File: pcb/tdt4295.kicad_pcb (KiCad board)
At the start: 6 copper layers, 94.8 x 111 mm, 158 parts, among them J1 DE15_Socket_HighDensity, J2 Conn_02x04_Odd_Even, J3 Conn_ST_STDC14, J4 Micro_SD_Card, J5 USB4110-GF-A, J6 USB4110-GF-A, SW1 SW_BLUE, SW2 SW_BLACK, U1 XC7A50T-FTG256, U2 410-251-B, U3 S70KL1283DPBHV020, U4 W25Q128JVS, U5 TPS54325PWP.d, U6 TPS54294PWP, U7 STM32U595ZJTx, U8 TPS2051CDBV, U9 USBLC6-2SC6, Y1 ASE-20MHz, Y2 16MHz

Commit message: pcb/layout: usbs and pds
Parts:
- removed C62, C71, C72, C74: 100nF, Capacitor_SMD:C_0805_2012Metric_Pad1.18x1.45mm_HandSolder
- removed C73: 1uF, Capacitor_SMD:C_0805_2012Metric_Pad1.18x1.45mm_HandSolder
- removed C75: 0.1uF, Capacitor_SMD:C_0805_2012Metric_Pad1.18x1.45mm_HandSolder
- removed C76: 150uF, Capacitor_SMD:C_0805_2012Metric_Pad1.18x1.45mm_HandSolder
- removed FB1: FerriteBead, Inductor_SMD:L_0805_2012Metric_Pad1.05x1.20mm_HandSolder
- removed J6: USB4110-GF-A, USB4110_GF_A:USB4110-GF-A_GCT
- removed R42, R43: 47, Resistor_SMD:R_0805_2012Metric_Pad1.20x1.40mm_HandSolder
- removed U9: USBLC6-2SC6, Package_TO_SOT_SMD:SOT-23-6
- added D5: green?, LED_SMD:LED_0805_2012Metric_Pad1.15x1.40mm_HandSolder, F.Cu at (55.5, 133.0)
- added D6: red?, LED_SMD:LED_0805_2012Metric_Pad1.15x1.40mm_HandSolder, F.Cu at (55.5, 130.0)
- added D7: LED_ARGB, LED_ARGB:SON4_APTF1616LSEEZGKQBKC_KNB, F.Cu at (263.4, 42.5)
- added D8: red, LED_SMD:LED_0805_2012Metric_Pad1.15x1.40mm_HandSolder, F.Cu at (55.4, 127.0)
- added J7: USB_C_Receptacle_USB2.0_14P, Connector_USB:USB_C_Receptacle_GCT_USB4105-xx-A_16P_TopMnt_Horizontal, F.Cu at (56.0, 116.0)
- added J8: USB_C_Receptacle_USB2.0_14P, Connector_USB:USB_C_Receptacle_GCT_USB4105-xx-A_16P_TopMnt_Horizontal, F.Cu at (56.0, 100.5)
- added R56: 22, Resistor_SMD:R_0805_2012Metric_Pad1.20x1.40mm_HandSolder, F.Cu at (253.8, 63.8)
- added R57: 1k, Resistor_SMD:R_0805_2012Metric_Pad1.20x1.40mm_HandSolder, F.Cu at (60.5, 127.0)
- added R58: 5.1k, Resistor_SMD:R_0805_2012Metric_Pad1.20x1.40mm_HandSolder, F.Cu at (65.0, 117.0)
- added R59: 5.1k, Resistor_SMD:R_0805_2012Metric_Pad1.20x1.40mm_HandSolder, F.Cu at (65.0, 114.0)
- added R60: 10k, Resistor_SMD:R_0805_2012Metric_Pad1.20x1.40mm_HandSolder, F.Cu at (76.0, 94.5)
- C10, C14, C16, C17, C20, C23, C26, C27, C28, C29, C30, C7, C8, C9: footprint Capacitor_SMD:C_0603_1608Metric_Pad1.08x0.95mm_HandSolder -> Capacitor_SMD:C_0805_2012Metric_Pad1.18x1.45mm_HandSolder; moved to F.Cu
- C11, C12, C13, C15, C18, C19, C21, C22, C24, C25, C3, C4, C5, C50, C51, C52, C53, C54, C55, C56, C57, C58, C59, C6, C60, C61, C66, C67, R51: moved to F.Cu
- C36, C37, C46, C47: moved to B.Cu
- C65: value 100nF -> 4.7uF; moved to F.Cu
- C68: value 1uF -> 100nF; moved to F.Cu
- C69: value 4.7uF -> 0.1uF; moved to F.Cu
- C70: value 1uF -> 150uF; moved to F.Cu
- D2: value green? -> blue?
- D4: value red -> blue?
- J1: value DE15_Socket_HighDensity -> FPGA_DEBUG; footprint Connector_Dsub:DSUB-15_Socket_EdgeMount_P2.77mm -> Connector_PinHeader_2.54mm:PinHeader_2x07_P2.54mm_Vertical
- J2: value Conn_02x04_Odd_Even -> DE15_Socket_HighDensity; footprint Connector_JST:JST_PUD_B08B-PUDSS_2x04_P2.00mm_Vertical -> Connector_Dsub:DSUB-15_Socket_EdgeMount_P2.77mm
- J3: value Conn_ST_STDC14 -> Conn_02x04_Odd_Even; footprint Connector_PinHeader_1.27mm:PinHeader_2x07_P1.27mm_Vertical_SMD -> Connector_JST:JST_PUD_B08B-PUDSS_2x04_P2.00mm_Vertical
- J4: value Micro_SD_Card -> Conn_ST_STDC14; footprint Connector_Card:microSD_HC_Molex_47219-2001 -> Connector_PinHeader_1.27mm:PinHeader_2x07_P1.27mm_Vertical_SMD
- J5: value USB4110-GF-A -> Micro_SD_Card; footprint USB4110_GF_A:USB4110-GF-A_GCT -> Connector_Card:microSD_HC_Molex_47219-2001
- R1: value 4.7k -> 10k
- R10: value 1.0k -> 1.1k
- R12: value 3.9k -> 18k
- R13: value 2.0k -> 9.1k
- R14: value 1.0k -> 4.3k
- R15: value 510 -> 2.2k
- R16: value 3.9k -> 1.1k
- R17: value 2.0k -> 560
- R18: value 1.0k -> 8.2k
- R19: value 510 -> 4.3k
- R2: value 330 -> 10k
- R20: value 100 -> 2.2k
- R21: value 100 -> 1.1k
- R22: value 4.7k -> 510
- R23: value 4.7k -> 1k
- R24: value 2.4k -> 1k
- R25: value 30.1k -> 4.7k
- R26: value 22.1k -> 4.7k
- R27: value 1k -> 2.4k
- R28: value 1k -> 51
- R29: value 6.81k -> 22
- R30: value 22.1k -> 22
- R31: value 100k -> 30.1k
- R32: value 100k -> 22.1k
- R33: value 73.2k -> 1k
- R34: value 22.1k -> 1k
- R35: value 1 -> 1k
- R36: value 330 -> 6.81k
- R37: value 100K -> 22.1k
- R38: value 1OK -> 100k; moved to F.Cu
- R39: value 22 -> 100k
- R4: value 4.7k -> 330
- R40: value 22 -> 73.2k
- R41: value 51 -> 22.1k
- R44: value 47 -> 1OK
- R45: value 47 -> 22
- R47: value 22 -> 51
- R48, R49: value 22 -> 47; moved to F.Cu
- R5, R6: value 10k -> 4.7k
- R50: value 22 -> 47
- R52: value 1k -> 22
- R53, R54: value 5.1k -> 22
- R55: value 10k -> 22
- R7: value 4.7k -> 8.2k
- R8: value 3.9k -> 4.3k
- R9: value 2.0k -> 2.2k
- U2: value 410-251-B -> S70KL1283DPBHV020; footprint 410_251_B:IC11_410-251-B_DGT -> S70KL1283DPBHV020:BGA24C100P5X5_600X800X100
- U3: value S70KL1283DPBHV020 -> W25Q128JVS; footprint S70KL1283DPBHV020:BGA24C100P5X5_600X800X100 -> Package_SO:SOIC-8_5.3x5.3mm_P1.27mm
- U4: value W25Q128JVS -> TPS54325PWP.d; footprint Package_SO:SOIC-8_5.3x5.3mm_P1.27mm -> TPS54325PWP.d:PWP14_2P31X2P46
- U5: value TPS54325PWP.d -> TPS54294PWP; footprint TPS54325PWP.d:PWP14_2P31X2P46 -> TPS54294PWP:PWP16_2P31X2P46
- U6: value TPS54294PWP -> STM32U595ZJTx; footprint TPS54294PWP:PWP16_2P31X2P46 -> Package_QFP:LQFP-144_20x20mm_P0.5mm
- U7: value STM32U595ZJTx -> TPS2051CDBV; footprint Package_QFP:LQFP-144_20x20mm_P0.5mm -> Package_TO_SOT_SMD:SOT-23-5
- U8: value TPS2051CDBV -> USBLC6-2SC6; footprint Package_TO_SOT_SMD:SOT-23-5 -> Package_TO_SOT_SMD:SOT-23-6
- moved J5 202.6 mm to (250.3, 32.8), turned to 0 degrees
- moved J4 188.2 mm to (261.0, 61.9), turned to 0 degrees
- moved R52 184.7 mm to (249.0, 66.8), turned to 0 degrees
- moved R54 181.1 mm to (253.8, 57.9)
- moved R55 181.0 mm to (253.8, 60.9), turned to 0 degrees
- moved R53 173.4 mm to (249.0, 69.7)
- moved U6 166.4 mm to (229.7, 37.0)
- moved Y2 162.9 mm to (258.1, 43.1)
- moved R49 156.3 mm to (249.0, 57.9), turned to 0 degrees
- moved R46 150.2 mm to (244.3, 63.8), turned to 0 degrees
- moved R47 149.5 mm to (244.3, 66.8), turned to 0 degrees
- moved R48 148.9 mm to (244.3, 69.7), turned to 0 degrees
- moved SW1 148.7 mm to (248.7, 44.7), turned to 0 degrees
- moved R50 145.0 mm to (249.0, 60.9), turned to 0 degrees
- moved R51 144.4 mm to (249.0, 63.8), turned to 0 degrees
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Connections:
- C38 pad 1: Net-(U6-VBST1) -> Net-(U5-VBST1)
- C38 pad 2: Net-(U6-SW1) -> Net-(U5-SW1)
- C39 pad 1: Net-(U5-SS) -> Net-(U4-SS)
- C40 pad 1: Net-(U5-VREG5) -> Net-(U4-VREG5)
- C41 pad 1: Net-(U5-SW1) -> Net-(U4-SW1)
- C41 pad 2: Net-(U5-VBST) -> Net-(U4-VBST)
- C42 pad 1: Net-(U6-VREG5) -> Net-(U5-VREG5)
- C43 pad 1: Net-(U6-VBST2) -> Net-(U5-VBST2)
- C43 pad 2: Net-(U6-SW2) -> Net-(U5-SW2)
- C48 pad 1: +3.3V -> +3V3
- C49 pad 1: +3.3V -> +3V3
- C50 pad 1: +3.3V -> +3V3
- C51 pad 1: +3.3V -> +3V3
- C52 pad 1: +3.3V -> +3V3
- C53 pad 1: +3.3V -> +3V3
- C54 pad 1: +3.3V -> +3V3
- C55 pad 1: +3.3V -> +3V3
- C56 pad 1: +3.3V -> +3V3
- C57 pad 1: +3.3V -> +3V3
- C58 pad 1: +3.3V -> +3V3
- C59 pad 1: +3.3V -> +3V3
- C60 pad 1: +3.3V -> +3V3
- C61 pad 1: +3.3V -> +3V3
- C63 pad 2: Net-(U7-PH0) -> Net-(U6-PH0)
- C64 pad 2: Net-(U7-PH1) -> Net-(U6-PH1)
- C65 pad 1: +3.3VA -> Net-(U6-VCAP)
- C66 pad 1: +3.3VA -> GND
- C66 pad 2: GND -> Net-(J4-~{RST})
- C67 pad 1: +3.3VA -> +3V3
- C68 pad 1: +3.3VA -> +3V3
- C69 pad 1: Net-(U7-VCAP) -> POWER_IN
- C70 pad 1: +3.3V -> Net-(U7-OUT)
- D3 pad 1: GND -> +3V3
- J1 pad 1: /fpga/RED_ANALOG -> GND
- J1 pad 10: GND -> /fpga/TDI_0
- J1 pad 11: unconnected-(J1-Pad11) -> GND
- J1 pad 13: /fpga/HSYNC -> GND
- J1 pad 14: /fpga/VSYNC -> unconnected-(J1-Pin_14-Pad14)
- J1 pad 2: /fpga/GREEN_ANALOG -> +3V3
- J1 pad 3: /fpga/BLUE_ANALOG -> GND
- J1 pad 4: unconnected-(J1-Pad4) -> /fpga/TMS_0
- J1 pad 6: GND -> /fpga/TCK_0
- J1 pad 8: GND -> /fpga/TDO_0
- J1 pad 9: unconnected-(J1-Pad9) -> GND
- J2 pad 1: POWER_IN -> /fpga/RED_ANALOG
- J2 pad 2: GND -> /fpga/GREEN_ANALOG
- J2 pad 3: +3.3V -> /fpga/BLUE_ANALOG
- J2 pad 4: GND -> unconnected-(J2-Pad4)
- J2 pad 5: +1V8 -> GND
- J2 pad 7: +1V0 -> GND
- J3 pad 1: unconnected-(J3-NC-Pad1) -> POWER_IN
- J3 pad 2: unconnected-(J3-NC-Pad2) -> GND
- J3 pad 3: +3.3V -> +1V0
- J3 pad 4: Net-(J3-JTMS/SWDIO) -> GND
- J3 pad 5: GND -> +1V8
- J3 pad 6: Net-(J3-JCLK/SWCLK) -> GND
- J3 pad 7: GND -> +3V3
- J3 pad 8: Net-(J3-JTDO/SWO) -> GND
- J4 pad 1: Net-(J4-DAT2) -> unconnected-(J4-NC-Pad1)
- J4 pad 2: Net-(J4-DAT3/CD) -> unconnected-(J4-NC-Pad2)
- J4 pad 3: Net-(J4-CMD) -> +3V3
- J4 pad 4: +3.3V -> Net-(J4-JTMS/SWDIO)
- J4 pad 5: Net-(J4-CLK) -> GND
- J4 pad 6: GND -> Net-(J4-JCLK/SWCLK)
- J4 pad 7: Net-(J4-DAT0) -> GND
- J4 pad 8: Net-(J4-DAT1) -> Net-(J4-JTDO/SWO)
- L1 pad 2: Net-(U6-SW1) -> Net-(U5-SW1)
- L2 pad 2: Net-(U5-SW1) -> Net-(U4-SW1)
- L3 pad 1: Net-(U6-SW2) -> Net-(U5-SW2)
- L3 pad 2: +3.3V -> +3V3
- R1 pad 1: Net-(U1C-M0_0) -> +3V3
- R1 pad 2: +3V3 -> /fpga/TMS_0
- R10 pad 2: Net-(U1B-IO_L9P_T1_DQS_34) -> Net-(U1B-IO_L8N_T1_34)
- R11 pad 2: Net-(U1B-IO_L8N_T1_34) -> Net-(U1B-IO_L8P_T1_34)
- R12 pad 2: Net-(U1B-IO_L8P_T1_34) -> Net-(U1B-IO_L7N_T1_34)
- R13 pad 2: Net-(U1B-IO_L7N_T1_34) -> Net-(U1B-IO_L7P_T1_34)
- R14 pad 2: Net-(U1B-IO_L7P_T1_34) -> Net-(U1B-IO_L6N_T0_VREF_34)
- R15 pad 2: Net-(U1B-IO_L6N_T0_VREF_34) -> Net-(U1B-IO_L6P_T0_34)
- R16 pad 1: /fpga/BLUE_ANALOG -> /fpga/GREEN_ANALOG
- R16 pad 2: Net-(U1B-IO_L6P_T0_34) -> Net-(U1B-IO_L5N_T0_34)
- R17 pad 1: /fpga/BLUE_ANALOG -> /fpga/GREEN_ANALOG
- R17 pad 2: Net-(U1B-IO_L5N_T0_34) -> Net-(U1B-IO_L5P_T0_34)
- R18 pad 2: Net-(U1B-IO_L5P_T0_34) -> Net-(U1B-IO_L4N_T0_34)
- R19 pad 2: Net-(U1B-IO_L4N_T0_34) -> Net-(U1B-IO_L4P_T0_34)
- R2 pad 1: done -> +3V3
- R2 pad 2: +3V3 -> /fpga/TCK_0
- R20 pad 1: /fpga/HSYNC -> /fpga/BLUE_ANALOG
- R20 pad 2: Net-(U1B-IO_L4P_T0_34) -> Net-(U1B-IO_L3N_T0_DQS_34)
- R21 pad 1: /fpga/VSYNC -> /fpga/BLUE_ANALOG
- R21 pad 2: Net-(U1B-IO_L3N_T0_DQS_34) -> Net-(U1B-IO_L3P_T0_DQS_34)
- R22 pad 1: +3V3 -> /fpga/BLUE_ANALOG
- R22 pad 2: Net-(U1A-IO_L2N_T0_D03_14) -> Net-(U1B-IO_L2N_T0_34)
- R23 pad 1: +3V3 -> FPGA_PROGRAM_B
- R23 pad 2: Net-(U1A-IO_L2P_T0_D02_14) -> Net-(D1-A)
- R24 pad 1: +3V3 -> FPGA_DONE
- R24 pad 2: Net-(U1A-IO_L6P_T0_FCS_B_14) -> Net-(D2-A)
- R25 pad 1: +1V8 -> +3V3
- R25 pad 2: Net-(U6-VFB1) -> Net-(U1A-IO_L2N_T0_D03_14)
- R26 pad 1: Net-(U6-VFB1) -> +3V3
- R26 pad 2: GND -> Net-(U1A-IO_L2P_T0_D02_14)
- R27 pad 1: +3.3V -> +3V3
- R27 pad 2: Net-(D1-A) -> Net-(U1A-IO_L6P_T0_FCS_B_14)
- R28 pad 1: +1V8 -> Net-(D3-Pad2)
- R28 pad 2: Net-(D2-A) -> Net-(U1A-IO_L2P_T0_AD8P_15)
- R29 pad 1: +1V0 -> Net-(D3-Pad3)
- R29 pad 2: Net-(U5-VFB) -> Net-(U1A-IO_L2N_T0_AD8N_15)
- R3 pad 1: Net-(U1C-INIT_B_0) -> Net-(U1C-M0_0)
- R30 pad 1: Net-(U5-VFB) -> Net-(D3-Pad4)
- R30 pad 2: GND -> Net-(U1A-IO_L3P_T0_DQS_AD1P_15)
- R31 pad 1: Net-(U5-PG) -> +1V8
- R31 pad 2: Net-(U5-VREG5) -> Net-(U5-VFB1)
- R32 pad 1: Net-(U6-VREG5) -> Net-(U5-VFB1)
- R32 pad 2: Net-(U6-EN2) -> GND
- R33 pad 1: +3.3V -> +3V3
- R33 pad 2: Net-(U6-VFB2) -> Net-(D4-A)
- R34 pad 1: Net-(U6-VFB2) -> +1V8
- R34 pad 2: GND -> Net-(D5-A)
- R35 pad 1: Net-(FB1-Pad2) -> +1V0
- R35 pad 2: +3.3VA -> Net-(D6-A)
- R36 pad 1: USER_BUTTON -> +1V0
- R36 pad 2: Net-(R36-Pad2) -> Net-(U4-VFB)
- R37 pad 1: Net-(R36-Pad2) -> Net-(U4-VFB)
- R37 pad 2: Net-(C62-Pad2) -> GND
- R38 pad 1: GND -> Net-(U4-PG)
- R38 pad 2: Net-(U7-PH3) -> Net-(U4-VREG5)
- R39 pad 1: Net-(D3-Pad4) -> Net-(U5-VREG5)
- R39 pad 2: Net-(U7-PE0) -> Net-(U5-EN2)
- R4 pad 1: program_b -> FPGA_DONE
- R40 pad 1: Net-(D3-Pad3) -> +3V3
- R40 pad 2: Net-(U7-PE1) -> Net-(U5-VFB2)
- R41 pad 1: Net-(D3-Pad2) -> Net-(U5-VFB2)
- R41 pad 2: Net-(U7-PE2) -> GND
- R44 pad 1: Net-(U7-PB3) -> GND
- R44 pad 2: Net-(J3-JTDO/SWO) -> Net-(U6-PH3)
- R45 pad 1: CC1 -> Net-(D7-Pad4)
- R45 pad 2: Net-(J3-JTDI/NC) -> Net-(U6-PE0)
- R46 pad 1: Net-(U7-PC10) -> Net-(D7-Pad3)
- R46 pad 2: Net-(J4-DAT2) -> Net-(U6-PE1)
- R47 pad 1: Net-(U7-PC11) -> Net-(D7-Pad2)
- R47 pad 2: Net-(J4-DAT3/CD) -> Net-(U6-PE2)
- R48 pad 1: SPI_MOSI -> /MCU/MCU_STLINK_JCLK
- R48 pad 2: Net-(J4-CMD) -> Net-(J4-JCLK/SWCLK)
- R49 pad 1: SPI_SCK -> /MCU/MCU_STLINK_JTMS
- R49 pad 2: Net-(J4-CLK) -> Net-(J4-JTMS/SWDIO)
- R5 pad 1: Net-(U1C-TCK_0) -> Net-(U1C-INIT_B_0)
- R50 pad 1: SPI_MISO -> /MCU/MCU_STLINK_JTDO
- R50 pad 2: Net-(J4-DAT0) -> Net-(J4-JTDO/SWO)
- R51 pad 1: Net-(U7-PC9) -> /MCU/SD_DAT2
- R51 pad 2: Net-(J4-DAT1) -> Net-(J5-DAT2)
- R52 pad 1: POWER_IN -> /MCU/SD_DAT3
- R52 pad 2: Net-(D4-A) -> Net-(J5-DAT3/CD)
- R53 pad 1: Net-(J5-CC2) -> /MCU/SD_CMD
- R53 pad 2: GND -> Net-(J5-CMD)
- R54 pad 1: Net-(J5-CC1) -> /MCU/SD_CLK
- R54 pad 2: GND -> Net-(J5-CLK)
- R55 pad 1: fault_signal -> /MCU/SD_DAT0
- R55 pad 2: POWER_IN -> Net-(J5-DAT0)
- R6 pad 1: Net-(U1C-TMS_0) -> FPGA_PROGRAM_B
- R7 pad 1: Net-(U1C-TDI_0) -> /fpga/RED_ANALOG
- R7 pad 2: +3V3 -> Net-(U1B-IO_L10P_T1_34)
- R8 pad 2: Net-(U1B-IO_L10P_T1_34) -> Net-(U1B-IO_L9N_T1_DQS_34)
- R9 pad 2: Net-(U1B-IO_L9N_T1_DQS_34) -> Net-(U1B-IO_L9P_T1_DQS_34)
- SW1 pad 1: +3.3V -> USER_BUTTON
- SW1 pad 2: Net-(R36-Pad2) -> GND
- SW2 pad 1: Net-(J3-~{RST}) -> Net-(J4-~{RST})
- U1 pad A8: unconnected-(U1A-IO_L2P_T0_AD8P_15-PadA8) -> Net-(U1A-IO_L2P_T0_AD8P_15)
- U1 pad A9: unconnected-(U1A-IO_L2N_T0_AD8N_15-PadA9) -> Net-(U1A-IO_L2N_T0_AD8N_15)
- U1 pad B9: unconnected-(U1A-IO_L3P_T0_DQS_AD1P_15-PadB9) -> Net-(U1A-IO_L3P_T0_DQS_AD1P_15)
- U1 pad H10: done -> FPGA_DONE
- U1 pad L6: +3.3V -> +3V3
- U1 pad L7: Net-(U1C-TCK_0) -> /fpga/TMS_0
- U1 pad L9: program_b -> FPGA_PROGRAM_B
- U1 pad M1: unconnected-(U1B-IO_L2N_T0_34-PadM1) -> Net-(U1B-IO_L2N_T0_34)
- U1 pad M2: unconnected-(U1B-IO_L2P_T0_34-PadM2) -> /fpga/HSYNC
- U1 pad M4: unconnected-(U1B-IO_L1N_T0_34-PadM4) -> /fpga/VSYNC
- U1 pad M7: Net-(U1C-TMS_0) -> /fpga/TCK_0
- U1 pad N3: unconnected-(U1B-IO_L3P_T0_DQS_34-PadN3) -> Net-(U1B-IO_L3P_T0_DQS_34)
- U1 pad N7: Net-(U1C-TDI_0) -> /fpga/TDI_0
- U1 pad N8: Net-(U1C-TDO_0) -> /fpga/TDO_0
- U4 pad 1: Net-(U1A-IO_L6P_T0_FCS_B_14) -> +1V0
- U4 pad 2: Net-(U1A-IO_L1N_T0_D01_DIN_14) -> Net-(U4-VFB)
- U4 pad 3: Net-(U1A-IO_L2P_T0_D02_14) -> Net-(U4-VREG5)
- U4 pad 4: GND -> Net-(U4-SS)
- U4 pad 5: Net-(U1A-IO_L1P_T0_D00_MOSI_14) -> GND
- U4 pad 6: Net-(U1C-CCLK_0) -> Net-(U4-PG)
- U4 pad 7: Net-(U1A-IO_L2N_T0_D03_14) -> POWER_IN
- U4 pad 8: +3V3 -> GND
- U5 pad 1: +1V0 -> POWER_IN
- U5 pad 10: Net-(U5-SW1) -> Net-(U5-VFB2)
- U5 pad 11: Net-(U5-SW1) -> unconnected-(U5-PG2-Pad11)
- U5 pad 12: Net-(U5-VBST) -> Net-(U5-EN2)
- U5 pad 13: POWER_IN -> GND
- U5 pad 14: POWER_IN -> Net-(U5-SW2)
- U5 pad 15: GND -> Net-(U5-VBST2)
- U5 pad 2: Net-(U5-VFB) -> Net-(U5-VBST1)
- U5 pad 3: Net-(U5-VREG5) -> Net-(U5-SW1)
- U5 pad 4: Net-(U5-SS) -> GND
- U5 pad 5: GND -> Net-(U4-PG)
- U5 pad 6: Net-(U5-PG) -> Net-(U5-EN2)
- U5 pad 7: POWER_IN -> Net-(U5-VFB1)
- U5 pad 9: GND -> Net-(U5-VREG5)
- U6 pad 1: POWER_IN -> Net-(U6-PE2)
- U6 pad 10: Net-(U6-VFB2) -> P2_IO0
- U6 pad 11: unconnected-(U6-PG2-Pad11) -> P2_IO1
- U6 pad 12: Net-(U6-EN2) -> P2_IO2
- U6 pad 13: GND -> P2_IO3
- U6 pad 14: Net-(U6-SW2) -> P2_CLK
- U6 pad 15: Net-(U6-VBST2) -> unconnected-(U6-PF5-Pad15)
- U6 pad 16: POWER_IN -> GND
- U6 pad 2: Net-(U6-VBST1) -> unconnected-(U6-PE3-Pad2)
- U6 pad 3: Net-(U6-SW1) -> unconnected-(U6-PE4-Pad3)
- U6 pad 4: GND -> unconnected-(U6-PE5-Pad4)
- U6 pad 5: Net-(U5-PG) -> unconnected-(U6-PE6-Pad5)
- U6 pad 6: Net-(U6-EN2) -> +3V3
- U6 pad 7: Net-(U6-VFB1) -> USER_BUTTON
- U6 pad 8: GND -> unconnected-(U6-PC14-Pad8)
- U6 pad 9: Net-(U6-VREG5) -> unconnected-(U6-PC15-Pad9)
- U7 pad 1: Net-(U7-PE2) -> Net-(U7-OUT)
- U7 pad 2: unconnected-(U7-PE3-Pad2) -> GND
- U7 pad 3: unconnected-(U7-PE4-Pad3) -> fault_signal
- U7 pad 4: unconnected-(U7-PE5-Pad4) -> Drive_VBUS
- U7 pad 5: unconnected-(U7-PE6-Pad5) -> POWER_IN
- U8 pad 3: fault_signal -> Net-(J8-D--PadA7)
- U8 pad 4: Drive_VBUS -> USB_FS_N
- U8 pad 5: POWER_IN -> Net-(U7-OUT)
- Y2 pad 1: Net-(U7-PH0) -> Net-(U6-PH0)
- Y2 pad 3: Net-(U7-PH1) -> Net-(U6-PH1)
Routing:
- net GND: track 306.4 -> 110.4 mm, vias 137 -> 36
- net +3.3V: track 136.5 -> 0.00 mm, vias 23 -> 0
- net CC1: track 106.0 -> 0.00 mm, vias 4 -> 0
- net Net-(U7-PA13): track 69.7 -> 0.00 mm, vias 2 -> 0
- net P1_NCS: track 68.5 -> 0.00 mm, vias 2 -> 0
- net Net-(U1C-TDI_0): track 65.0 -> 0.00 mm, vias 2 -> 0
- net P2_NCS: track 64.5 -> 0.00 mm, vias 3 -> 0
- net Net-(J3-~{RST}): track 63.3 -> 0.00 mm, vias 1 -> 0
- net Net-(U7-PA14): track 62.6 -> 0.00 mm, vias 2 -> 0
- net SPI1_SCK: track 62.1 -> 0.00 mm, vias 3 -> 0
- net Net-(U1C-TDO_0): track 61.8 -> 0.00 mm, vias 2 -> 0
- net Net-(J3-VCP_TX): track 60.9 -> 0.00 mm, vias 2 -> 0
- net +3V3: track 79.6 -> 20.7 mm, vias 37 -> 2
- net Net-(J3-VCP_RX): track 58.8 -> 0.00 mm, vias 2 -> 0
- net /fpga/RED_ANALOG: track 58.5 -> 0.00 mm
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- removed copper zone on In2.Cu, net +3.3V
- removed copper zone on In2.Cu, net +3V3
- removed copper zone on In1.Cu, net GND
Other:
- board outline removed
- board text added: "1V0"
- board text added: "1V8"
- board text added: "3V3"
- board text added: "5V0"

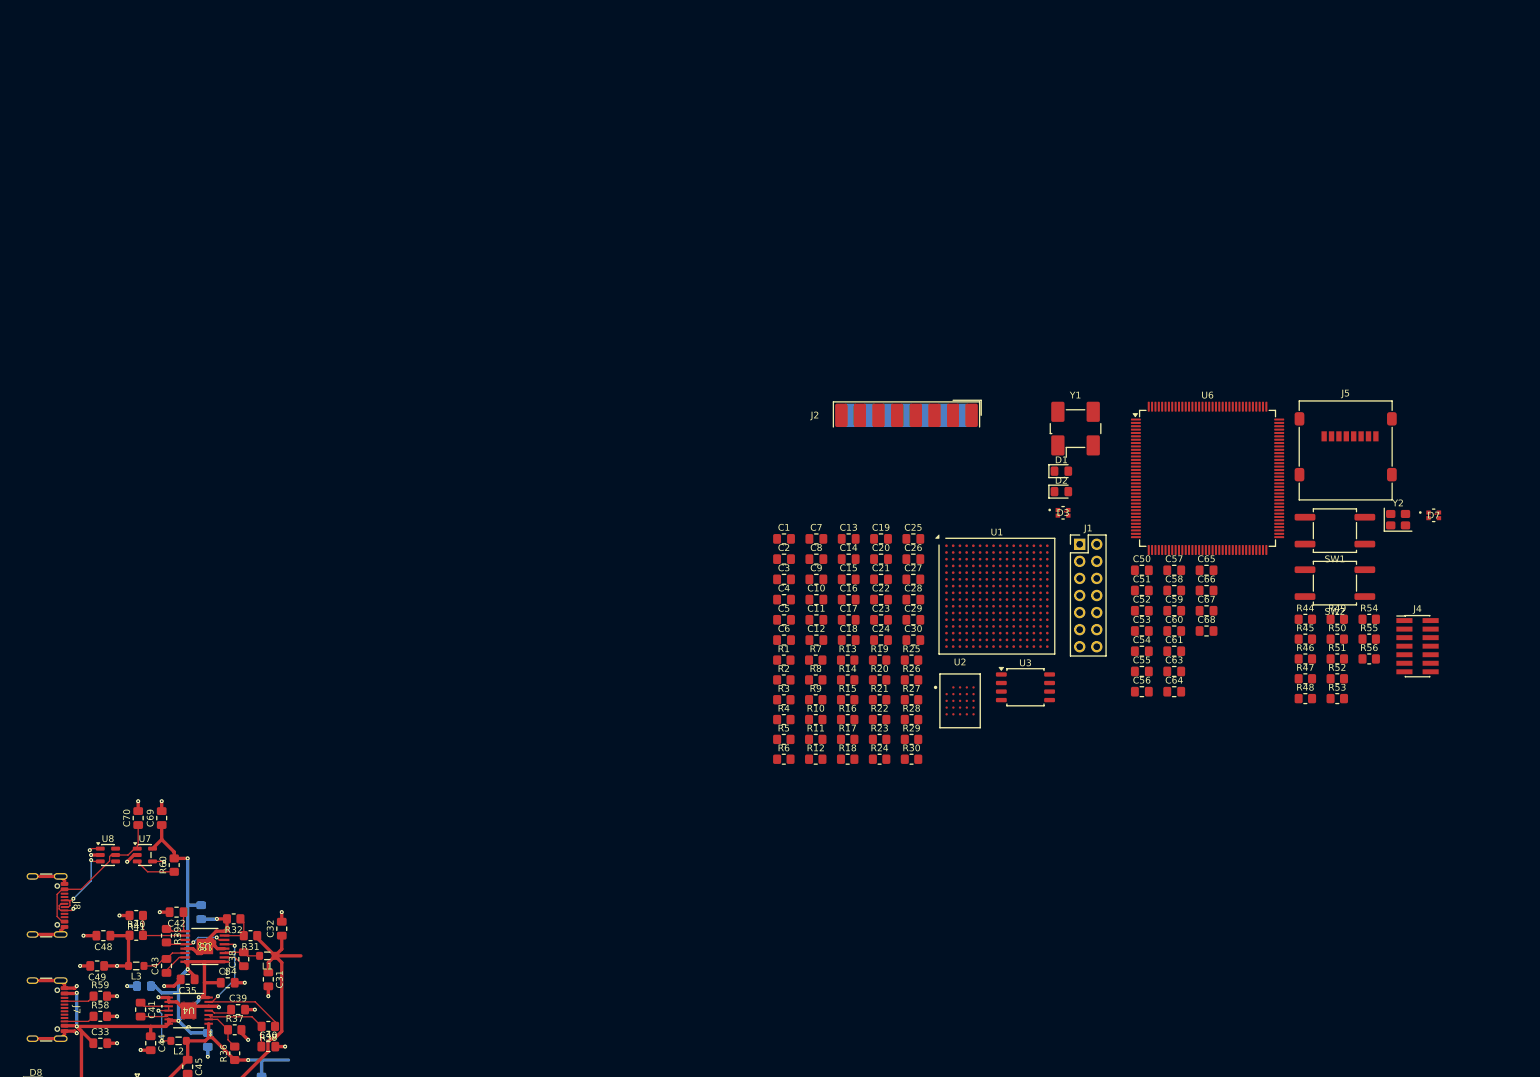
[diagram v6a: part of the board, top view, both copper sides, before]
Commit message: pcb: wip fan out dog bone
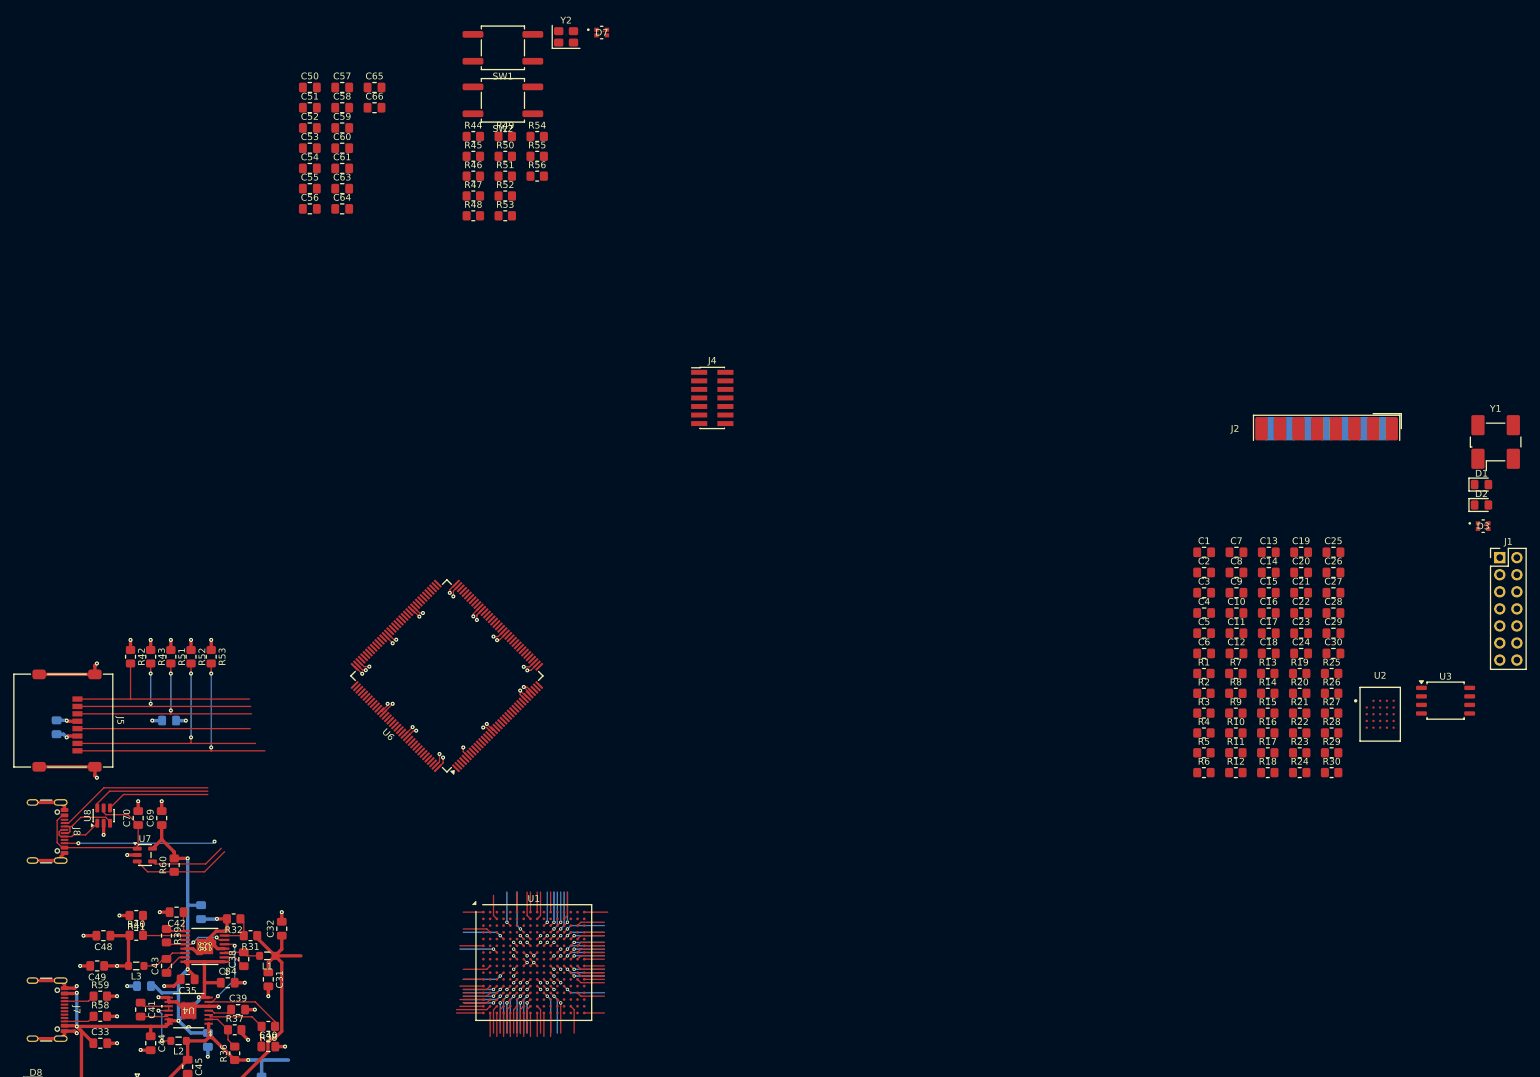
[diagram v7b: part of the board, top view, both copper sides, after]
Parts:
- added R42: 47k, Resistor_SMD:R_0805_2012Metric_Pad1.20x1.40mm_HandSolder, F.Cu at (69.5, 63.5)
- added R43: 47k, Resistor_SMD:R_0805_2012Metric_Pad1.20x1.40mm_HandSolder, F.Cu at (72.5, 63.5)
- added R51: 47k, Resistor_SMD:R_0805_2012Metric_Pad1.20x1.40mm_HandSolder, F.Cu at (75.5, 63.5)
- added R52: 47k, Resistor_SMD:R_0805_2012Metric_Pad1.20x1.40mm_HandSolder, F.Cu at (78.5, 63.5)
- added R53: 47k, Resistor_SMD:R_0805_2012Metric_Pad1.20x1.40mm_HandSolder, F.Cu at (81.5, 63.5)
- C67, C68: moved to B.Cu
- moved J5 195.0 mm to (59.5, 73.0), turned to -90 degrees
- moved C68 171.7 mm to (58.5, 74.0), turned to -90 degrees
- moved C67 155.2 mm to (75.2, 73.0)
- moved D7 143.1 mm to (139.6, -29.4)
- moved C50 143.1 mm to (96.2, -21.2)
- moved C51 143.1 mm to (96.2, -18.2)
- moved C52 143.1 mm to (96.2, -15.2)
- moved C53 143.1 mm to (96.2, -12.2)
- moved C54 143.1 mm to (96.2, -9.15)
- moved C55 143.1 mm to (96.2, -6.14)
- moved C56 143.1 mm to (96.2, -3.13)
- moved C57 143.1 mm to (101.0, -21.2)
- moved C58 143.1 mm to (101.0, -18.2)
- moved C59 143.1 mm to (101.0, -15.2)
- moved C60 143.1 mm to (101.0, -12.2)
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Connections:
- J5 pad 1: Net-(J5-DAT2) -> /MCU/SD_DAT2
- J5 pad 2: Net-(J5-DAT3/CD) -> /MCU/SD_DAT3
- J5 pad 3: Net-(J5-CMD) -> /MCU/SD_CMD
- J5 pad 5: Net-(J5-CLK) -> /MCU/SD_CLK
- J5 pad 7: Net-(J5-DAT0) -> /MCU/SD_DAT0
- J5 pad 8: Net-(J5-DAT1) -> /MCU/SD_DAT1
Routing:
- net GND: track 110.4 -> 373.8 mm, vias 36 -> 77
- net +3V3: track 20.7 -> 146.0 mm, vias 2 -> 32
- net +1V0: track 44.2 -> 102.6 mm, vias 1 -> 8
- net /MCU/SD_DAT1: track 0.00 -> 40.9 mm, vias 0 -> 2
- net /MCU/SD_DAT0: track 0.00 -> 38.4 mm, vias 0 -> 2
- net /MCU/SD_CMD: track 0.00 -> 33.4 mm, vias 0 -> 2
- net /MCU/SD_DAT3: track 0.00 -> 32.2 mm, vias 0 -> 2
- net /MCU/SD_DAT2: track 0.00 -> 30.9 mm
- net /MCU/SD_CLK: track 0.00 -> 25.7 mm
- net CC1: track 0.00 -> 23.5 mm
- net CC2: track 0.00 -> 22.4 mm, vias 0 -> 2
- net USB_FS_P: track 0.00 -> 17.9 mm
- net +1V8: track 63.8 -> 80.6 mm, vias 0 -> 2
- net USB_FS_N: track 0.00 -> 15.4 mm
- net Drive_VBUS: track 1.75 -> 11.3 mm, vias 1 -> 0
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
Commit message: pcb: wip layout
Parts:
- moved J1 194.6 mm to (97.8, 133.0), turned to 90 degrees
- moved U2 151.2 mm to (111.0, 117.0)
- moved R1 141.5 mm to (99.5, 122.5)
- moved R2 141.5 mm to (99.5, 125.5)
- moved U3 131.8 mm to (136.5, 98.5), turned to 90 degrees
- moved J2 130.5 mm to (152.0, 118.5), turned to 90 degrees
- moved D2 126.5 mm to (150.0, 79.3), turned to 180 degrees
- moved D3 125.4 mm to (153.2, 87.9)
- moved R10 123.7 mm to (124.2, 131.9)
- moved R11 123.7 mm to (124.2, 134.9)
- moved R12 123.7 mm to (124.2, 137.8)
- moved R13 123.7 mm to (129.0, 123.1)
- moved R14 123.7 mm to (129.0, 126.0)
- moved R15 123.7 mm to (129.0, 129.0)
- moved R16 123.7 mm to (129.0, 131.9)
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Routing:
- net GND: track 373.8 -> 272.9 mm, vias 77 -> 95
- net +3V3: track 146.0 -> 98.7 mm, vias 32 -> 40
- net +1V0: track 102.6 -> 72.8 mm, vias 8 -> 3
- net FPGA_DONE: track 0.00 -> 12.1 mm, vias 0 -> 2
- net Net-(U1C-INIT_B_0): track 0.00 -> 11.1 mm, vias 0 -> 2
- net Net-(D1-A): track 0.00 -> 3.45 mm
- net Net-(D2-A): track 0.00 -> 2.95 mm
- net +1V8: track 80.6 -> 83.2 mm, vias 2 -> 3
